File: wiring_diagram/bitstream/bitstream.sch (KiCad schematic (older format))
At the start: 19 parts

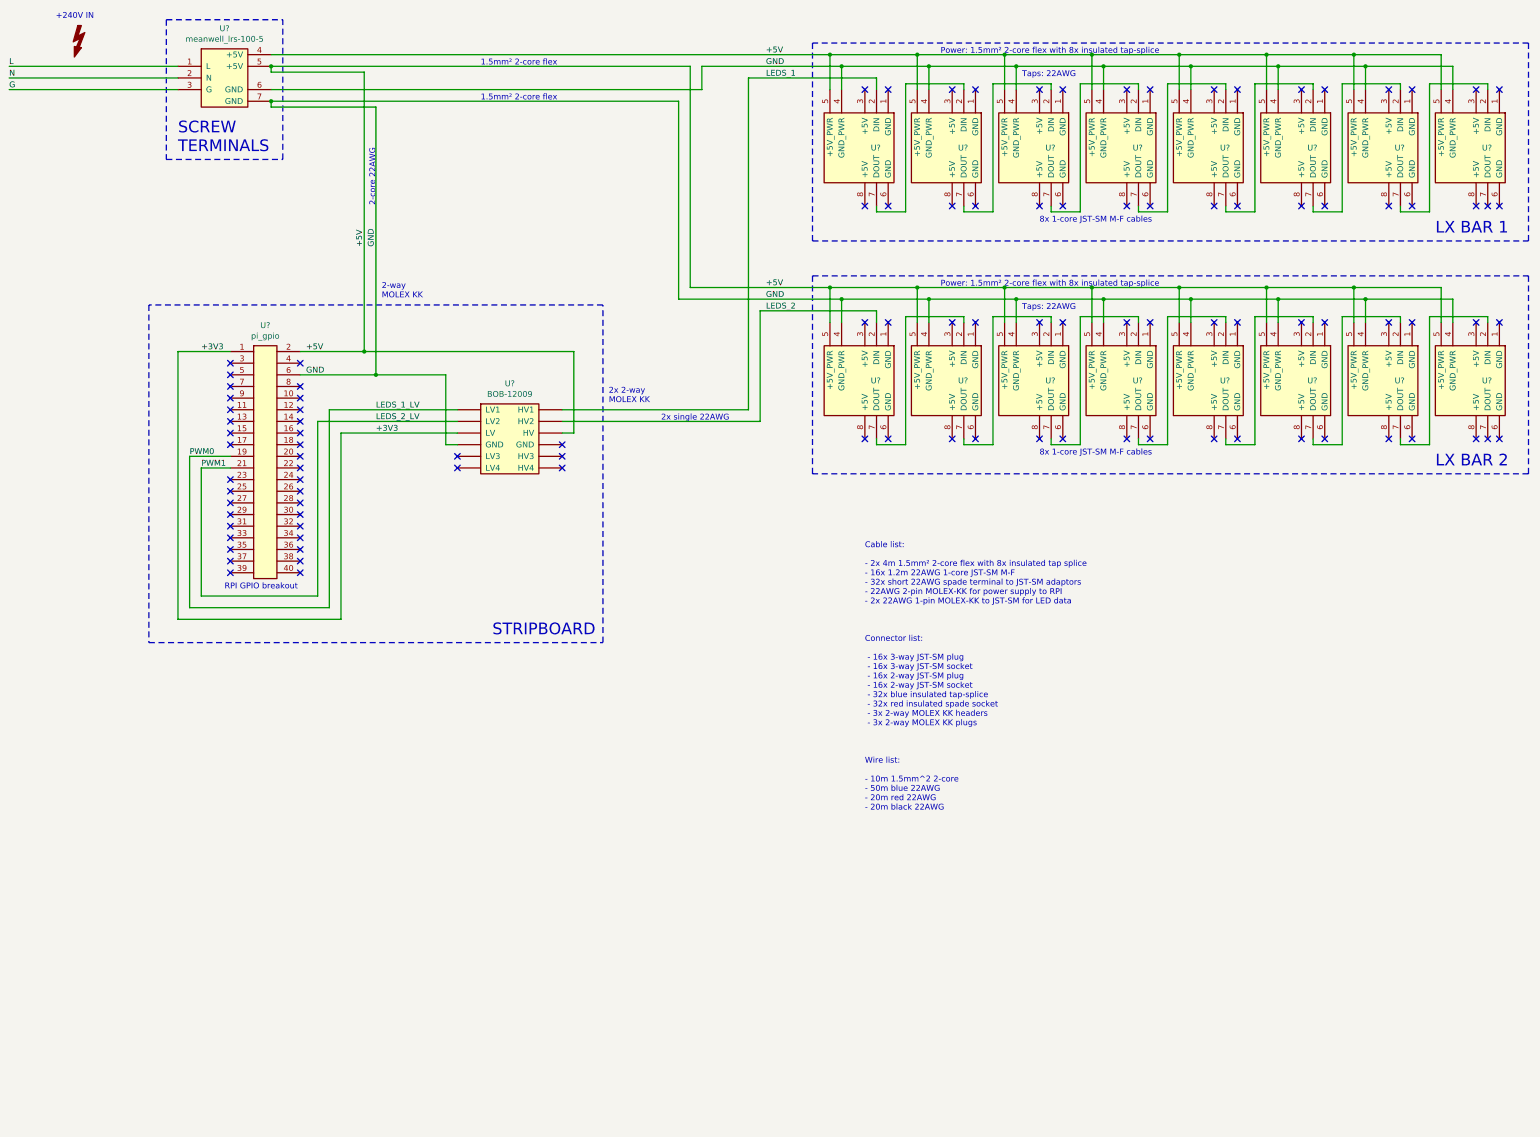
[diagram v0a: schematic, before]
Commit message: Update wiring diagram
Comments from Adam on signal current loops (added some extra ground
connections)
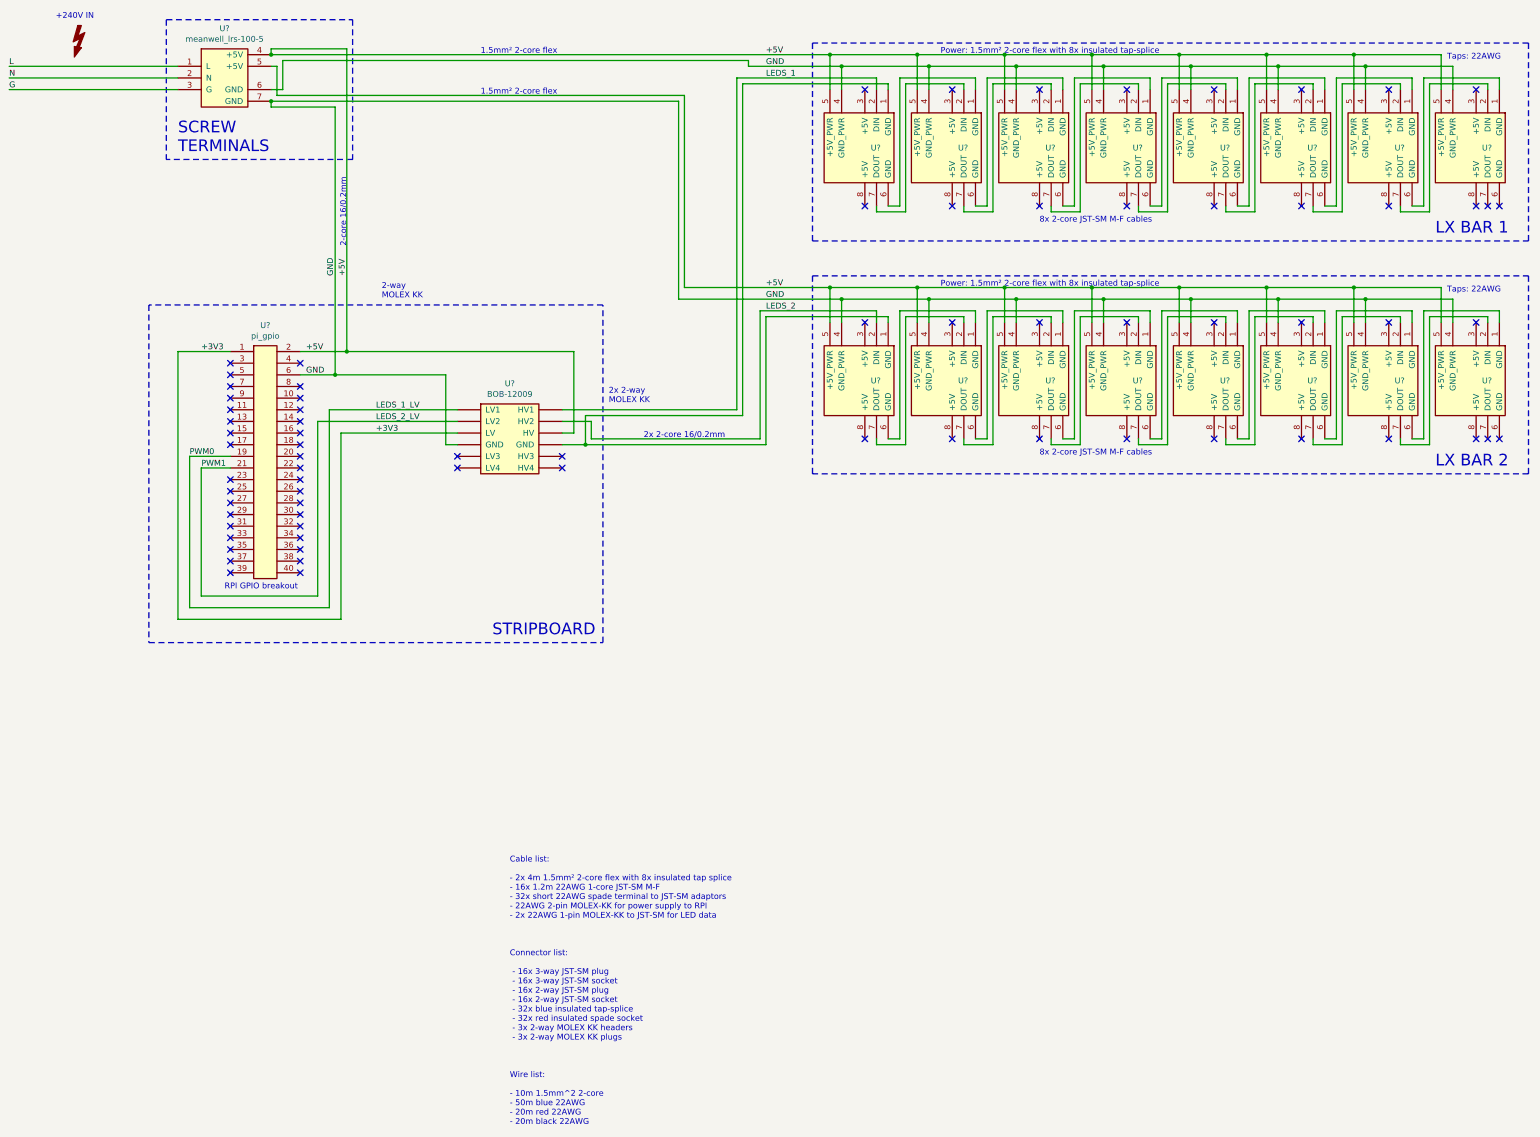
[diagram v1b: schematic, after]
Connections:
- net at U?.1 (GND): now also U?.1 (GND), U?.~ (LV4)
- net at U?.6 (GND): now also U?.1 (GND) (x14)
- no-connect marks 106 -> 75
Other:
- note added: "2-core 16/0.2mm"
- note added: "2x 2-core 16/0.2mm"
- note added: "8x 2-core JST-SM M-F cables"
- note removed: "2-core 22AWG"
- note removed: "2x single 22AWG"
- note removed: "8x 1-core JST-SM M-F cables"

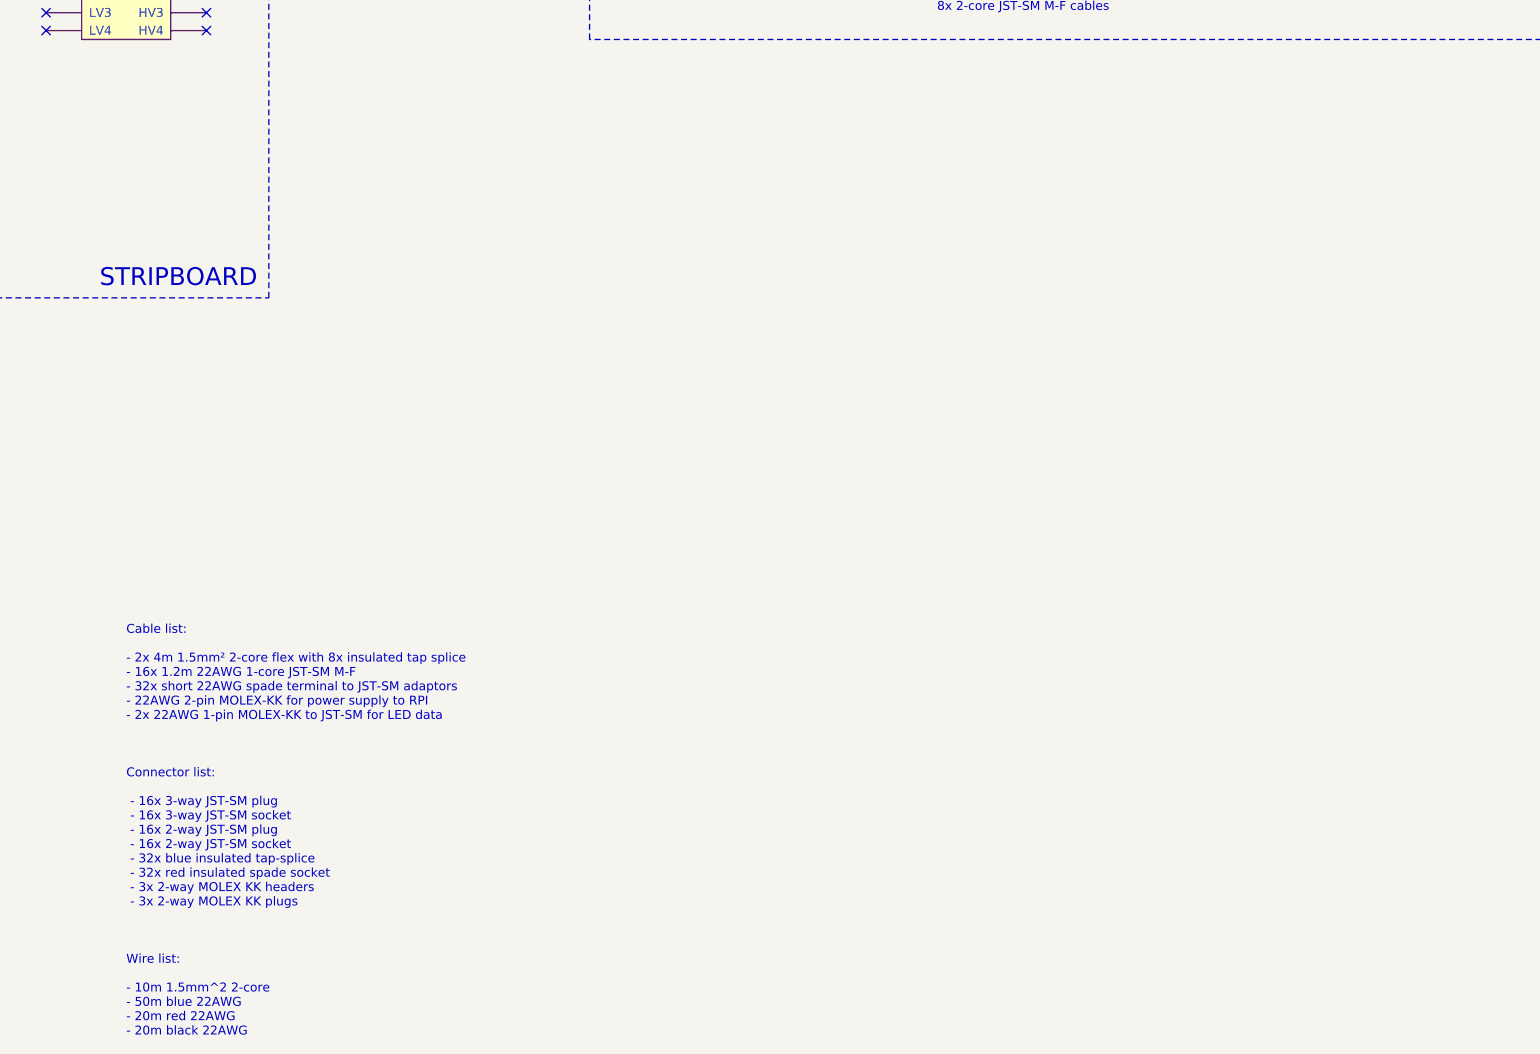
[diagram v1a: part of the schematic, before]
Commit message: Update cables inventory
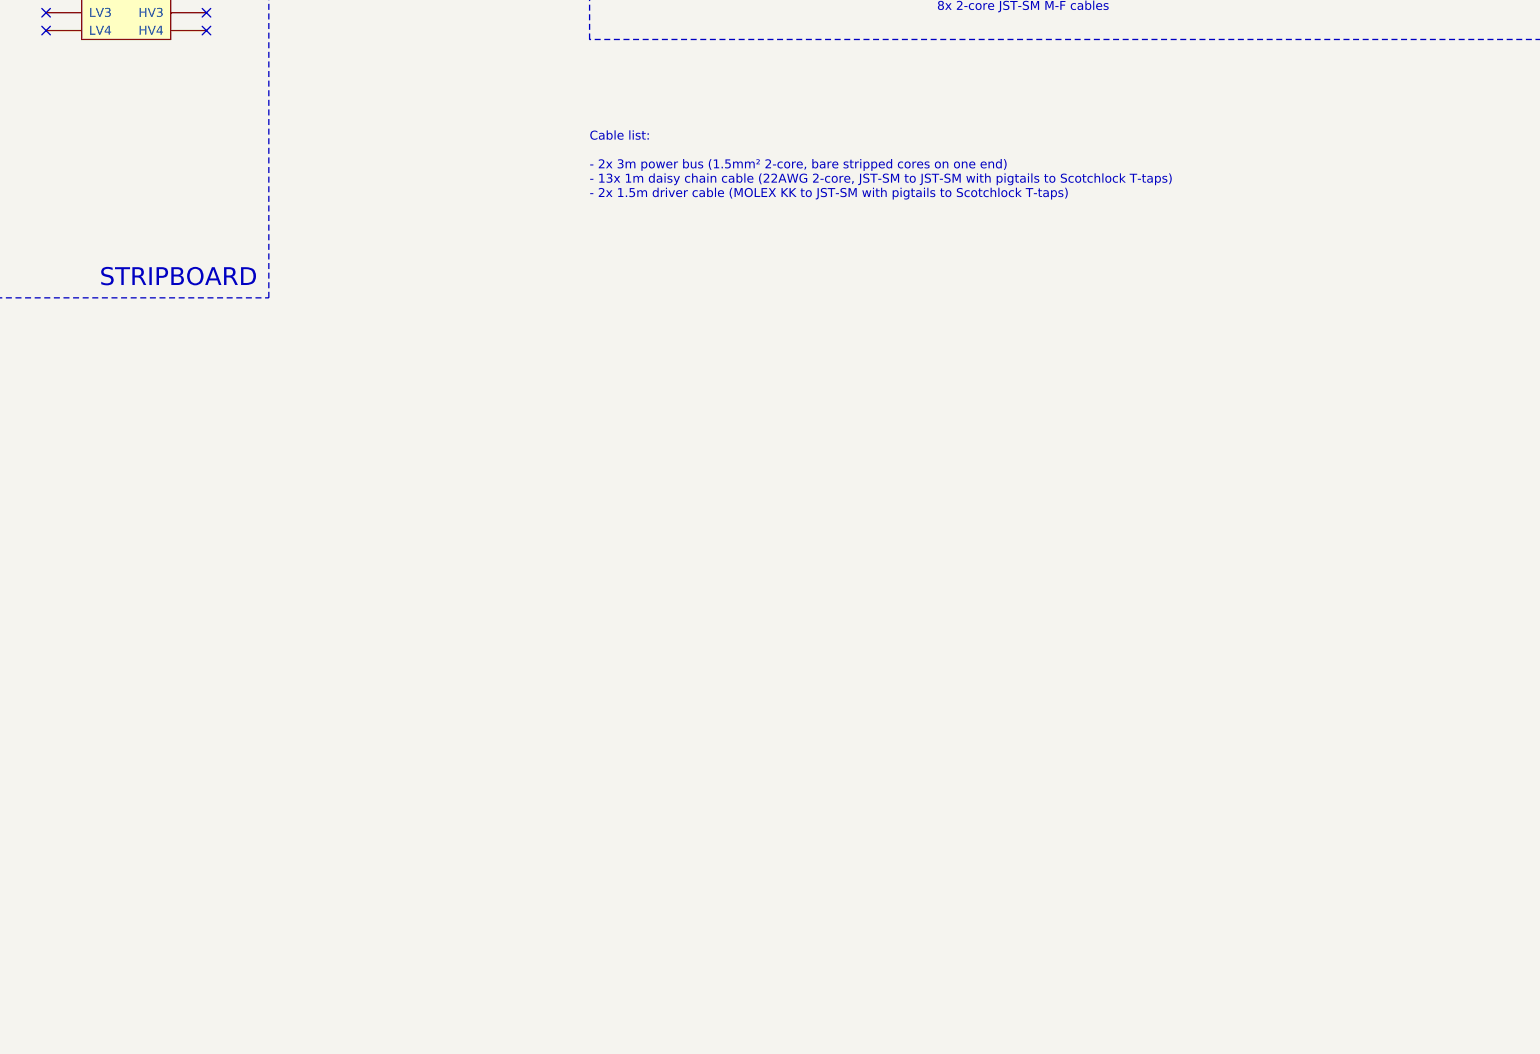
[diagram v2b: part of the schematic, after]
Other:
- note added: "Cable list:\n\n- 2x 3m power bus (1.5mm² 2-core, bare stripped cores on one end)\n- 13x 1m daisy chain cable (22AWG 2-core, JST-SM to JST-SM with pigtails to Scotchlock T-taps)\n- 2x 1.5m driver cable (MOLEX KK to JST-SM with pigtails to Scotchlock T-taps)"
- note removed: "Cable list:\n\n- 2x 4m 1.5mm² 2-core flex with 8x insulated tap splice\n- 16x 1.2m 22AWG 1-core JST-SM M-F\n- 32x short 22AWG spade terminal to JST-SM adaptors\n- 22AWG 2-pin MOLEX-KK for power supply to RPI\n- 2x 22AWG 1-pin MOLEX-KK to JST-SM for LED data\n\n\n\nConnector list:\n\n - 16x 3-way JST-SM plug\n - 16x 3-way JST-SM socket\n - 16x 2-way JST-SM plug\n - 16x 2-way JST-SM socket\n - 32x 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"
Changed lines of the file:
@@
 Text Notes 10500 4450 0    50   ~ 0
 8x 2-core JST-SM M-F cables
-Text Notes 5950 10200 0    50   ~ 0
-Cable list:\n\n- 2x 4m 1.5mm² 2-core flex with 8x insulated tap splice\n- 16x 1.2m 22AWG 1-core JST-SM M-F\n- 32x short 22AWG spade terminal to JST-SM adaptors\n- 22AWG 2-pin MOLEX-KK for power supply to RPI\n- 2x 22AWG 1-pin MOLEX-KK to JST-SM for LED data\n\n\n\nConnector list:\n\n - 16x 3-way JST-SM plug\n - 16x 3-way JST-SM socket\n - 16x 2-way JST-SM plug\n - 16x 2-way JST-SM socket\n - 32x blue insulated tap-splice\n - 32x red insulated spade socket\n - 3x 2-way MOLEX KK headers\n - 3x 2-way MOLEX KK plugs\n\n\n\nWire list:\n\n- 10m 1.5mm^2 2-core\n- 50m blue 22AWG\n- 20m red 22AWG\n- 20m black 22AWG
+Text Notes 8550 5500 0    50   ~ 0
+Cable list:\n\n- 2x 3m power bus (1.5mm² 2-core, bare stripped cores on one end)\n- 13x 1m daisy chain cable (22AWG 2-core, JST-SM to JST-SM with pigtails to Scotchlock T-taps)\n- 2x 1.5m driver cable (MOLEX KK to JST-SM with pigtails to Scotchlock T-taps)
 NoConn ~ 3550 3650
 NoConn ~ 3550 3750
